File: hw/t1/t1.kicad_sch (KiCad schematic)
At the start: 62 parts, among them J1 SFP edge (INF-8074i), J2 Rosenberger E6S20A-40MT5-Z (H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, U1 DP83TG720S-Q1 (or DP83TC812S-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, U2 STM32G031F6P6, U3 TPS62822DLC, Y1 25MHz CL8pF 2016

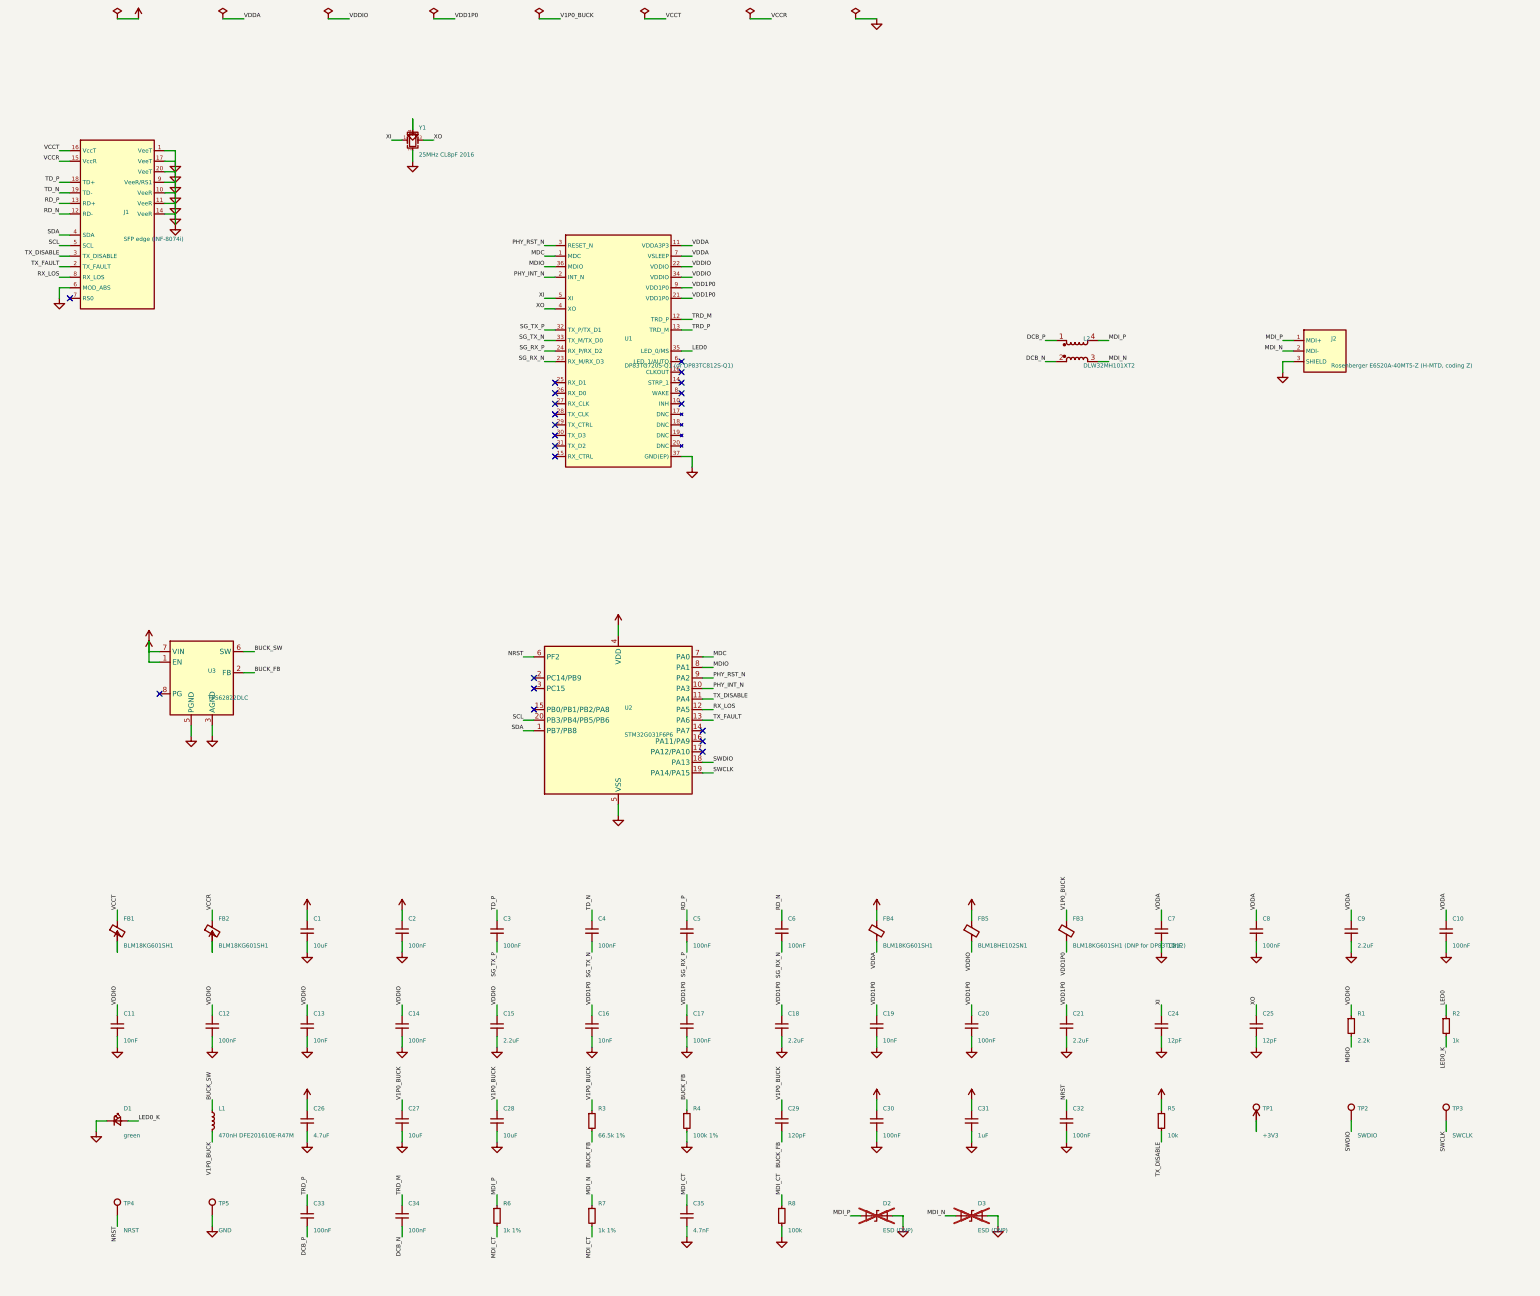
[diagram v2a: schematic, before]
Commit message: t1: opens clean in KiCad 9 - schematic parity, linked footprints, check script
A KiCad 9 check (official Docker image, as a reviewer would open it) found
what KiCad 7's python and kicad-cli could not test:
- no footprint was linked to its schematic symbol: KiCad's Update PCB
  would have replaced every part. Footprints now carry /<symbol uuid>
  plus Sheetname/Sheetfile
- 140 net-name conflicts: local labels name nets /TD_P on the root sheet,
  the board says TD_P. The schematic now uses global labels
- no-connect pins are nets of their own in KiCad
  (unconnected-(REF-PIN-PadN)); the pads now carry them
- DNP/BOM flags agreed nowhere (ESD diodes, test pads): excluded from the
  BOM on both sides (KiCad 7 boards have no DNP attribute)
- back-side label was not mirrored
- the buck's footprint is gone from KiCad 9's library: vendored into
  hw/fp/sfp.pretty

Result (sh hw/check_kicad9.sh t1): DRC 0 errors / 0 unconnected, parity
clean, ERC 0 errors; the only warnings are KiCad 9's newer library copies.
Copper is unchanged (tracks, vias, pads and fills compared item by item);
gerber/CPL/BOM changes are ordering only. KiCad 7 ERC 0/0, DRC 0/0.
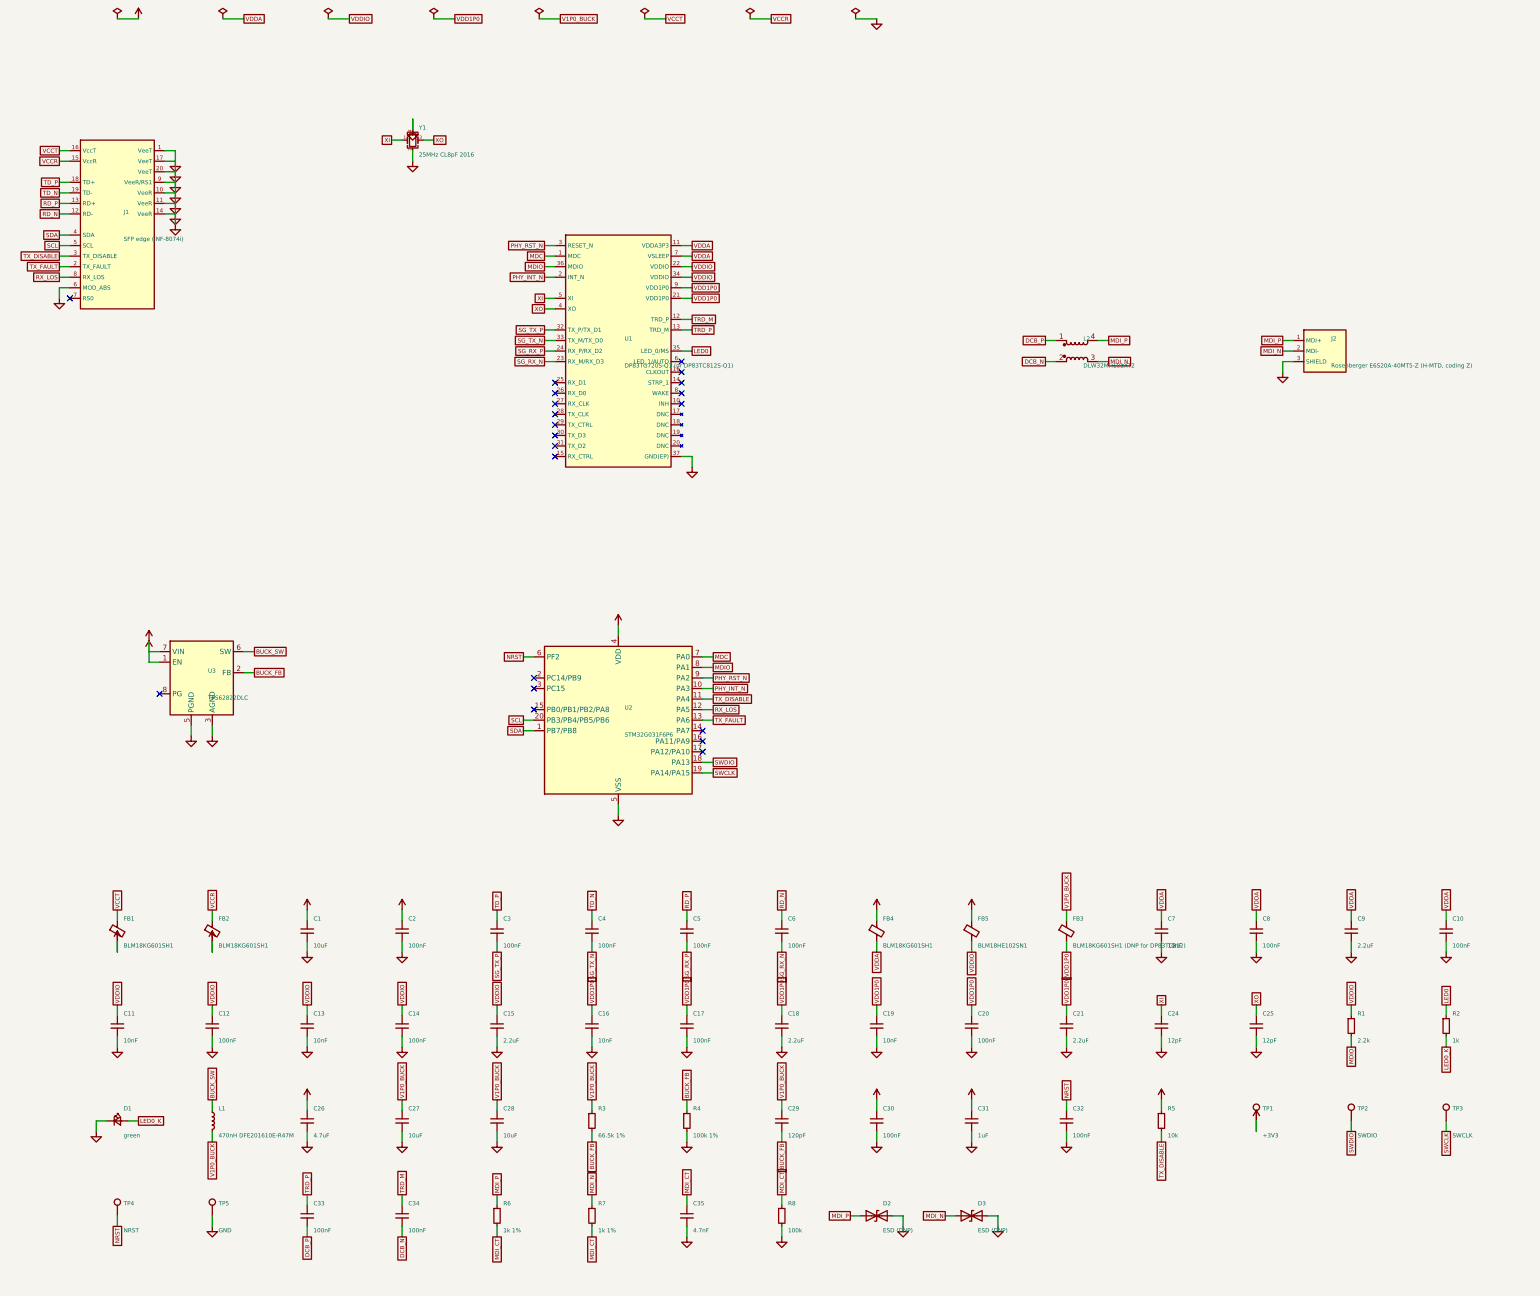
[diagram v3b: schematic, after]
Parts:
- D2, D3: now fitted; now left out of the parts list
- TP1, TP2, TP3, TP4, TP5: now left out of the parts list
- U3: footprint Package_DFN_QFN:Texas_VSON-HR-8_1.5x2mm_P0.5mm -> sfp:Texas_VSON-HR-8_1.5x2mm_P0.5mm

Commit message: t1: design-review fixes - coupled pairs by hand, F/GND/GND/B, load switch, two BOMs, CI
- every SGMII/MDI pair laid coupled (0.114/0.152, ~100 ohm diff) on one layer
  with matched vias; router does the slow nets only. Worst skew 1.08 mm (SG_RX)
- In2 is GND; slow signals may cross it except under the bottom-side pair
- SGMII lanes laid straight, polarity inverted in the PHY by the firmware
  (SGMII_CTRL_1 bits 7/8, TG720 and TC812)
- TPS22918 load switch on the 3.3 V entry (~3.6 ms soft start)
- 0.6 mm no-copper strip along every edge (mouse bites); escapes where it
  closed the router's way (U4 ON, MDC/INT/RST, VDD1P0, MCU GND, XO)
- jlc/bom.csv + cpl.csv replaced by bom/cpl-tg720 and bom/cpl-tc812
- fab/t1-1to1.pdf for the H-MTD print check
- KiCad 9: DRC 0, parity clean, ERC clean; only lib-revision warnings pass
- GitHub Actions: KiCad 9 check, firmware (4 variants, no warnings), gateware
- root README rewritten (11.8 mm body, current status, hardware-only checks)
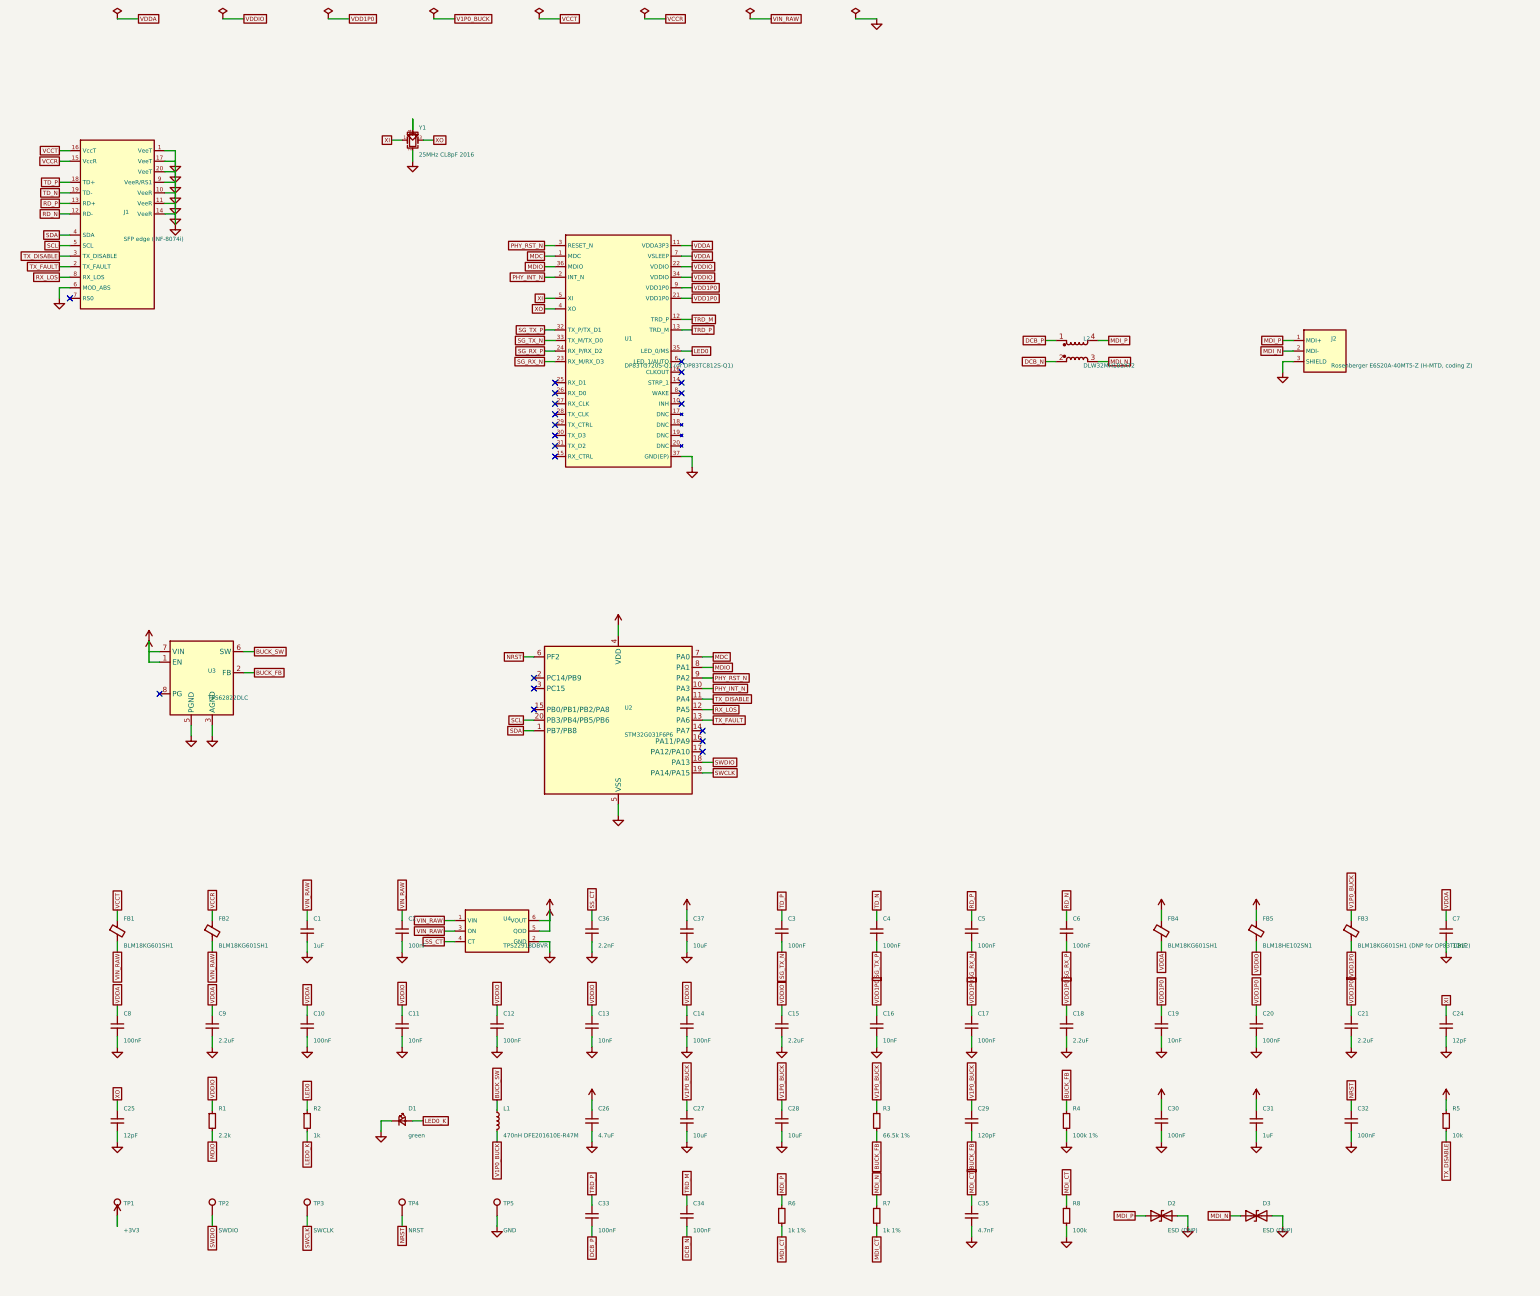
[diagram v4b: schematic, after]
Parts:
- added C36: 2.2nF, Capacitor_SMD:C_0402_1005Metric, symbol Device:C_Small
- added C37: 10uF, Capacitor_SMD:C_0603_1608Metric, symbol Device:C_Small
- added U4: TPS22918DBVR, Package_TO_SOT_SMD:SOT-23-6, symbol sfp:TPS22918
- C1: value 10uF -> 1uF; footprint Capacitor_SMD:C_0603_1608Metric -> Capacitor_SMD:C_0402_1005Metric; LCSC C19702 -> C52923
- R6, R7: footprint Resistor_SMD:R_0603_1608Metric -> Resistor_SMD:R_0402_1005Metric; LCSC C21190 -> C11702
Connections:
- net +3V3: now also C37.1, U4.5 (QOD), U4.6 (VOUT); no longer C1.1, C2.1, FB1.2, FB2.2
- net GND: now also C36.2, C37.2, U4.2 (GND)
- net SG_RX_N: now also C5.2; no longer C6.2
- net SG_RX_P: now also C6.2; no longer C5.2
- net SG_TX_N: now also C3.2; no longer C4.2
- net SG_TX_P: now also C4.2; no longer C3.2
- new net SS_CT: C36.1, U4.4 (CT)
- new net VIN_RAW: C1.1, C2.1, FB1.2, FB2.2, U4.1 (VIN), U4.3 (ON)
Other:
- moved on the sheet: C10, C11, C12, C13, C14, C15, C16, C17, C18, C19, C20, C21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

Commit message: RJ45: 6-layer board routed and clean, JLC panel and order sheet
- rj45: DRC 0 / 0 unconnected (KiCad 7 and 9), parity clean, ERC 0/0;
  gerbers, BOM/CPL, 1:1 print; 5-board panel with hand-placed tabs,
  checked with the board's own rules; ORDER.md with cost estimate
- sfpgen: side-pin power stubs clear the next pin's label (they shorted
  +3V3 to AVDD33 in the RJ45 schematic); project min via / hole clearance
  from the design
- t1: schematic regenerated with the stub fix, KiCad 9 re-checked
- CI: rj45 joins the KiCad 9 matrix
- t1s: work in progress (6 layers, not yet fully routed)
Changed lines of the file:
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@@
   (global_label "SS_CT" (shape passive) (at 118.11 252.73 180) (fields_autoplaced) (effects (font (size 1.0 1.0)) (justify right))
     (property "Intersheetrefs" "${INTERSHEET_REFS}" (at 118.11 252.73 0) (effects (font (size 1.0 1.0)) hide)))
-  (wire (pts (xy 140.97 247.65) (xy 143.51 247.65)) (stroke (width 0) (type default)))
-  (wire (pts (xy 143.51 247.65) (xy 143.51 245.11)) (stroke (width 0) (type default)))
-  (symbol (lib_id "power:+3V3") (at 143.51 245.11 0) (unit 1)
-    (in_bom no) (on_board yes) (dnp no)
-    (property "Reference" "#PWR011" (at 145.01 242.11 0) (effects (font (size 1.0 1.0)) (justify left) hide))
-    (property "Value" "+3V3" (at 145.01 248.61 0) (effects (font (size 1.0 1.0)) (justify left) hide))
-    (property "Footprint" "" (at 143.51 245.11 0) (effects (font (size 1.0 1.0)) hide))
-    (property "Datasheet" "" (at 143.51 245.11 0) (effects (font (size 1.0 1.0)) hide))
+  (wire (pts (xy 140.97 247.65) (xy 146.05 247.65)) (stroke (width 0) (type default)))
+  (wire (pts (xy 146.05 247.65) (xy 146.05 245.11)) (stroke (width 0) (type default)))
+  (symbol (lib_id "power:+3V3") (at 146.05 245.11 0) (unit 1)
+    (in_bom no) (on_board yes) (dnp no)
+    (property "Reference" "#PWR011" (at 147.55 242.11 0) (effects (font (size 1.0 1.0)) (justify left) hide))
+    (property "Value" "+3V3" (at 147.55 248.61 0) (effects (font (size 1.0 1.0)) (justify left) hide))
+    (property "Footprint" "" (at 146.05 245.11 0) (effects (font (size 1.0 1.0)) hide))
+    (property "Datasheet" "" (at 146.05 245.11 0) (effects (font (size 1.0 1.0)) hide))
     (pin "1")
     (instances (project "t1" (path "/8a4b1f2e-6c7d-4e8f-9a0b-1c2d3e4f5061" (reference "#PWR011") (unit 1))))
   )
-  (wire (pts (xy 140.97 250.19) (xy 143.51 250.19)) (stroke (width 0) (type default)))
-  (wire (pts (xy 143.51 250.19) (xy 143.51 247.65)) (stroke (width 0) (type default)))
-  (symbol (lib_id "power:+3V3") (at 143.51 247.65 0) (unit 1)
-    (in_bom no) (on_board yes) (dnp no)
-    (property "Reference" "#PWR012" (at 145.01 244.65 0) (effects (font (size 1.0 1.0)) (justify left) hide))
-    (property "Value" "+3V3" (at 145.01 251.15 0) (effects (font (size 1.0 1.0)) (justify left) hide))
-    (property "Footprint" "" (at 143.51 247.65 0) (effects (font (size 1.0 1.0)) hide))
-    (property "Datasheet" "" (at 143.51 247.65 0) (effects (font (size 1.0 1.0)) hide))
+  (wire (pts (xy 140.97 250.19) (xy 146.05 250.19)) (stroke (width 0) (type default)))
+  (wire (pts (xy 146.05 250.19) (xy 146.05 247.65)) (stroke (width 0) (type default)))
+  (symbol (lib_id "power:+3V3") (at 146.05 247.65 0) (unit 1)
+    (in_bom no) (on_board yes) (dnp no)
+    (property "Reference" "#PWR012" (at 147.55 244.65 0) (effects (font (size 1.0 1.0)) (justify left) hide))
+    (property "Value" "+3V3" (at 147.55 251.15 0) (effects (font (size 1.0 1.0)) (justify left) hide))
+    (property "Footprint" "" (at 146.05 247.65 0) (effects (font (size 1.0 1.0)) hide))
+    (property "Datasheet" "" (at 146.05 247.65 0) (effects (font (size 1.0 1.0)) hide))
     (pin "1")
     (instances (project "t1" (path "/8a4b1f2e-6c7d-4e8f-9a0b-1c2d3e4f5061" (reference "#PWR012") (unit 1))))
@@
     (instances (project "t1" (path "/8a4b1f2e-6c7d-4e8f-9a0b-1c2d3e4f5061" (reference "U3") (unit 1))))
   )
-  (wire (pts (xy 49.53 185.42) (xy 46.99 185.42)) (stroke (width 0) (type default)))
-  (wire (pts (xy 46.99 185.42) (xy 46.99 182.88)) (stroke (width 0) (type default)))
-  (symbol (lib_id "power:+3V3") (at 46.99 182.88 0) (unit 1)
-    (in_bom no) (on_board yes) (dnp no)
-    (property "Reference" "#PWR040" (at 48.49 179.88 0) (effects (font (size 1.0 1.0)) (justify left) hide))
-    (property "Value" "+3V3" (at 48.49 186.38 0) (effects (font (size 1.0 1.0)) (justify left) hide))
-    (property "Footprint" "" (at 46.99 182.88 0) (effects (font (size 1.0 1.0)) hide))
-    (property "Datasheet" "" (at 46.99 182.88 0) (effects (font (size 1.0 1.0)) hide))
+  (wire (pts (xy 49.53 185.42) (xy 44.45 185.42)) (stroke (width 0) (type default)))
+  (wire (pts (xy 44.45 185.42) (xy 44.45 182.88)) (stroke (width 0) (type default)))
+  (symbol (lib_id "power:+3V3") (at 44.45 182.88 0) (unit 1)
+    (in_bom no) (on_board yes) (dnp no)
+    (property "Reference" "#PWR040" (at 45.95 179.88 0) (effects (font (size 1.0 1.0)) (justify left) hide))
+    (property "Value" "+3V3" (at 45.95 186.38 0) (effects (font (size 1.0 1.0)) (justify left) hide))
+    (property "Footprint" "" (at 44.45 182.88 0) (effects (font (size 1.0 1.0)) hide))
+    (property "Datasheet" "" (at 44.45 182.88 0) (effects (font (size 1.0 1.0)) hide))
     (pin "1")
     (instances (project "t1" (path "/8a4b1f2e-6c7d-4e8f-9a0b-1c2d3e4f5061" (reference "#PWR040") (unit 1))))
@@
   (global_label "BUCK_SW" (shape passive) (at 72.39 182.88 0) (fields_autoplaced) (effects (font (size 1.0 1.0)) (justify left))
     (property "Intersheetrefs" "${INTERSHEET_REFS}" (at 72.39 182.88 0) (effects (font (size 1.0 1.0)) hide)))
-  (wire (pts (xy 49.53 182.88) (xy 46.99 182.88)) (stroke (width 0) (type default)))
-  (wire (pts (xy 46.99 182.88) (xy 46.99 180.34)) (stroke (width 0) (type default)))
-  (symbol (lib_id "power:+3V3") (at 46.99 180.34 0) (unit 1)
-    (in_bom no) (on_board yes) (dnp no)
-    (property "Reference" "#PWR043" (at 48.49 177.34 0) (effects (font (size 1.0 1.0)) (justify left) hide))
-    (property "Value" "+3V3" (at 48.49 183.84 0) (effects (font (size 1.0 1.0)) (justify left) hide))
-    (property "Footprint" "" (at 46.99 180.34 0) (effects (font (size 1.0 1.0)) hide))
-    (property "Datasheet" "" (at 46.99 180.34 0) (effects (font (size 1.0 1.0)) hide))
+  (wire (pts (xy 49.53 182.88) (xy 44.45 182.88)) (stroke (width 0) (type default)))
+  (wire (pts (xy 44.45 182.88) (xy 44.45 180.34)) (stroke (width 0) (type default)))
+  (symbol (lib_id "power:+3V3") (at 44.45 180.34 0) (unit 1)
+    (in_bom no) (on_board yes) (dnp no)
+    (property "Reference" "#PWR043" (at 45.95 177.34 0) (effects (font (size 1.0 1.0)) (justify left) hide))
+    (property "Value" "+3V3" (at 45.95 183.84 0) (effects (font (size 1.0 1.0)) (justify left) hide))
+    (property "Footprint" "" (at 44.45 180.34 0) (effects (font (size 1.0 1.0)) hide))
+    (property "Datasheet" "" (at 44.45 180.34 0) (effects (font (size 1.0 1.0)) hide))
     (pin "1")
     (instances (project "t1" (path "/8a4b1f2e-6c7d-4e8f-9a0b-1c2d3e4f5061" (reference "#PWR043") (unit 1))))
